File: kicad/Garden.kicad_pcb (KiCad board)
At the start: 2 copper layers, 24 parts, among them J1 EC, J10 FAN_PWM, J11 SPI, J2 TEMP, J3 DHT, J4 PH, J5 Serial, J6 Power, J7 RELAIS, J8 RC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

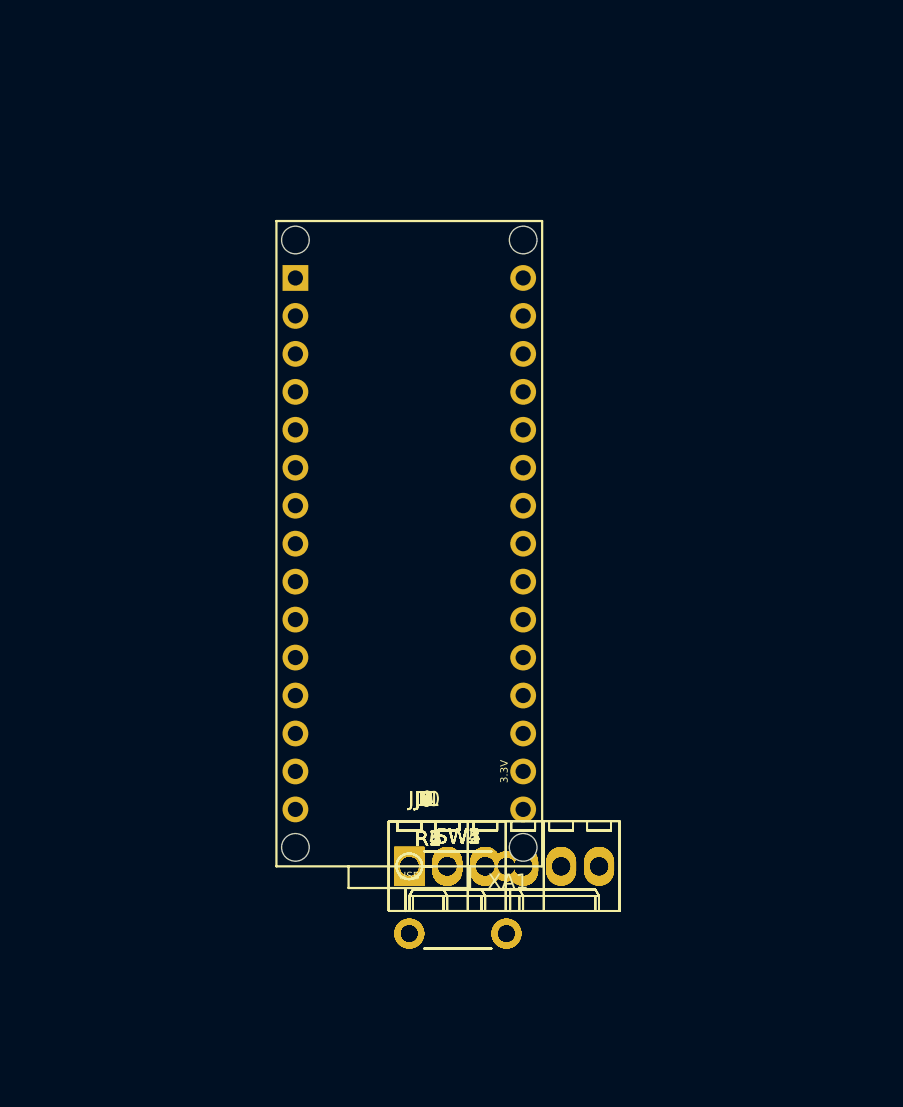
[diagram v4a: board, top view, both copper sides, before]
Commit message: Redesign board layout WIP
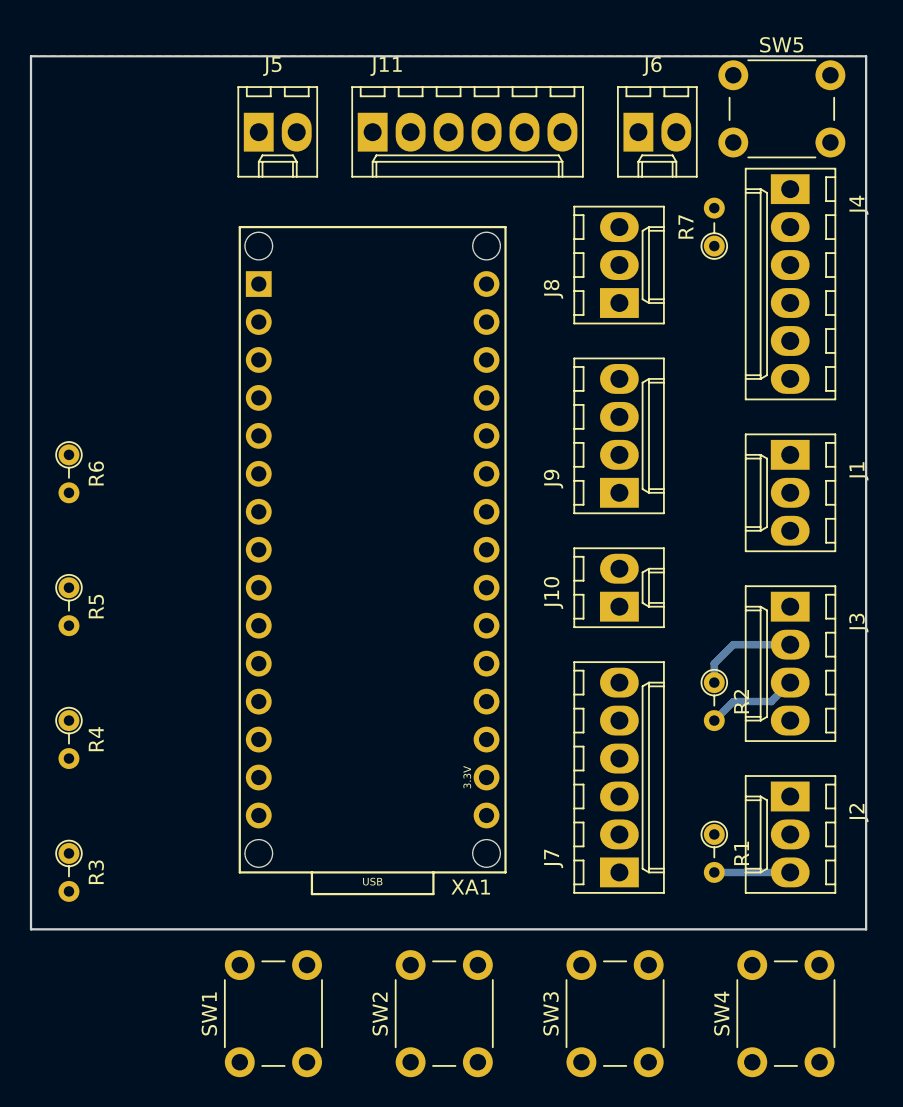
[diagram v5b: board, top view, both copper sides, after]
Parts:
- moved SW5 57.2 mm to (170.2, 52.1)
- moved J4 52.0 mm to (174.0, 59.7), turned to 270 degrees
- moved J6 51.5 mm to (163.8, 55.9)
- moved J5 50.1 mm to (138.4, 55.9)
- moved J11 49.2 mm to (146.1, 55.9)
- moved R7 46.3 mm to (168.9, 63.5), turned to 90 degrees
- moved J8 40.2 mm to (162.6, 67.3), turned to 90 degrees
- moved J1 37.5 mm to (174.0, 77.5), turned to 270 degrees
- moved R6 35.7 mm to (125.7, 77.5), turned to 270 degrees
- moved J3 30.8 mm to (174.0, 87.6), turned to 270 degrees
- moved R5 29.4 mm to (125.7, 86.4), turned to 270 degrees
- moved J9 28.7 mm to (162.6, 80.0), turned to 90 degrees
- moved SW4 26.4 mm to (171.4, 118.1), turned to 90 degrees
- moved J2 25.9 mm to (174.0, 100.3), turned to 270 degrees
- moved R4 24.8 mm to (125.7, 95.2), turned to 270 degrees
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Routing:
- net A0: track 0.00 -> 6.88 mm
- net Net-(J3-Pad3): track 0.00 -> 6.13 mm
- net D3: track 0.00 -> 5.08 mm
- added copper zone on F.Cu, net +5V
- added copper zone on B.Cu, net GND
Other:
- board outline added: 55.9 x 58.4 mm
- net class Default: trace_width 0.25 -> 0.5

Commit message: New pcb design with butons, wip
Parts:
- moved SW4 108.1 mm to (88.9, 48.3)
- moved SW3 91.9 mm to (100.3, 48.3)
- moved R2 86.8 mm to (86.4, 66.0)
- moved SW2 79.0 mm to (111.8, 48.3)
- moved J3 77.6 mm to (96.5, 83.8), turned to 180 degrees
- moved XA1 71.4 mm to (90.2, 61.0), turned to 270 degrees
- moved SW1 71.2 mm to (123.2, 48.3)
- moved J7 68.2 mm to (101.6, 74.9), turned to 180 degrees
- moved J1 67.6 mm to (106.7, 83.8), turned to 180 degrees
- moved R3 59.9 mm to (130.8, 44.5), turned to 90 degrees
- moved J4 55.1 mm to (124.5, 83.8), turned to 180 degrees
- moved J10 54.8 mm to (109.2, 74.9), turned to 180 degrees
- moved R4 51.2 mm to (119.4, 44.5), turned to 90 degrees
- moved R5 45.5 mm to (108.0, 44.5), turned to 90 degrees
- moved R6 44.1 mm to (96.5, 44.5), turned to 90 degrees
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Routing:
- net D13_SCK: track 0.00 -> 59.5 mm
- net D12_MISO: track 0.00 -> 58.7 mm
- net D11_MOSI: track 0.00 -> 55.1 mm
- net D10_CS: track 0.00 -> 52.8 mm
- net RX: track 0.00 -> 17.6 mm
- net TX: track 0.00 -> 14.3 mm
- net Net-(J3-Pad3): track 6.13 -> 17.6 mm
- net A0: track 6.88 -> 0.00 mm
- net D3: track 5.08 -> 11.4 mm
- net D2: track 0.00 -> 3.18 mm
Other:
- board size 55.9 x 58.4 mm -> 61 x 49.5 mm

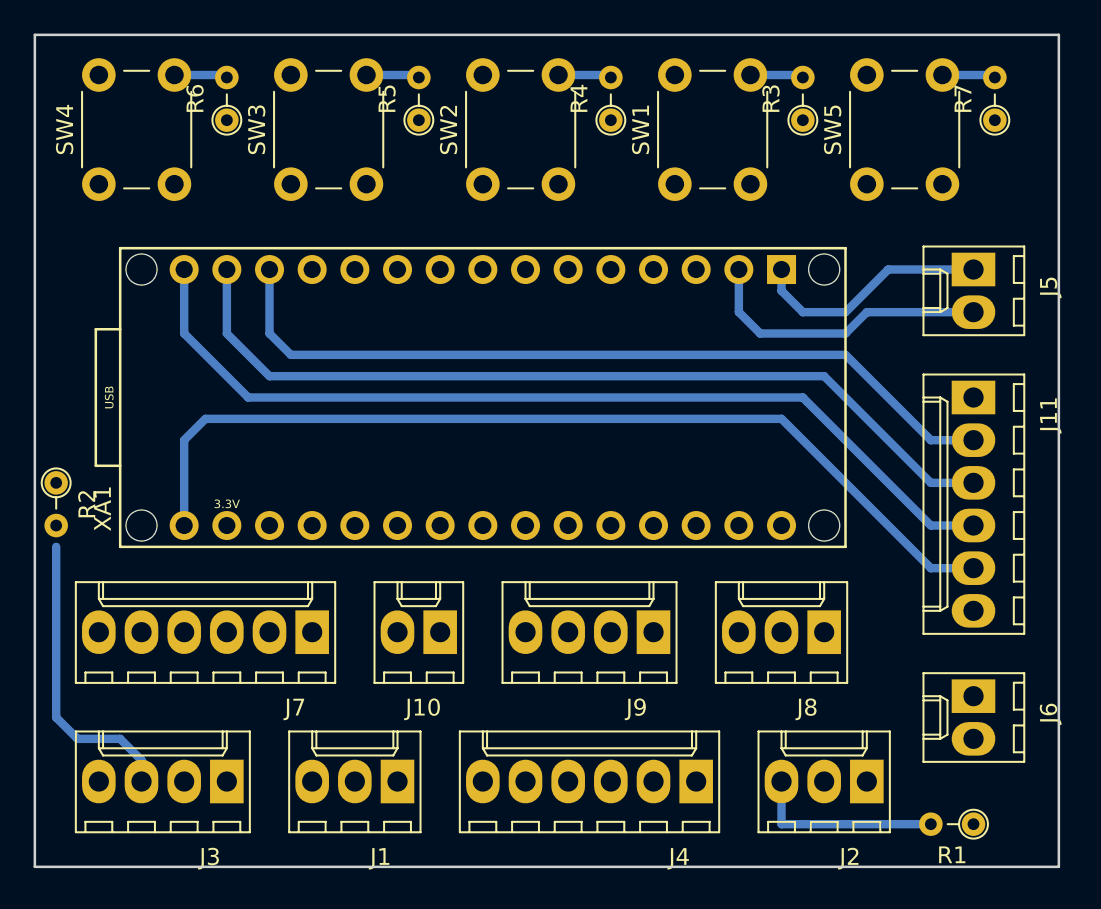
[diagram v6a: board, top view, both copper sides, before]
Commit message: Add missing tracks
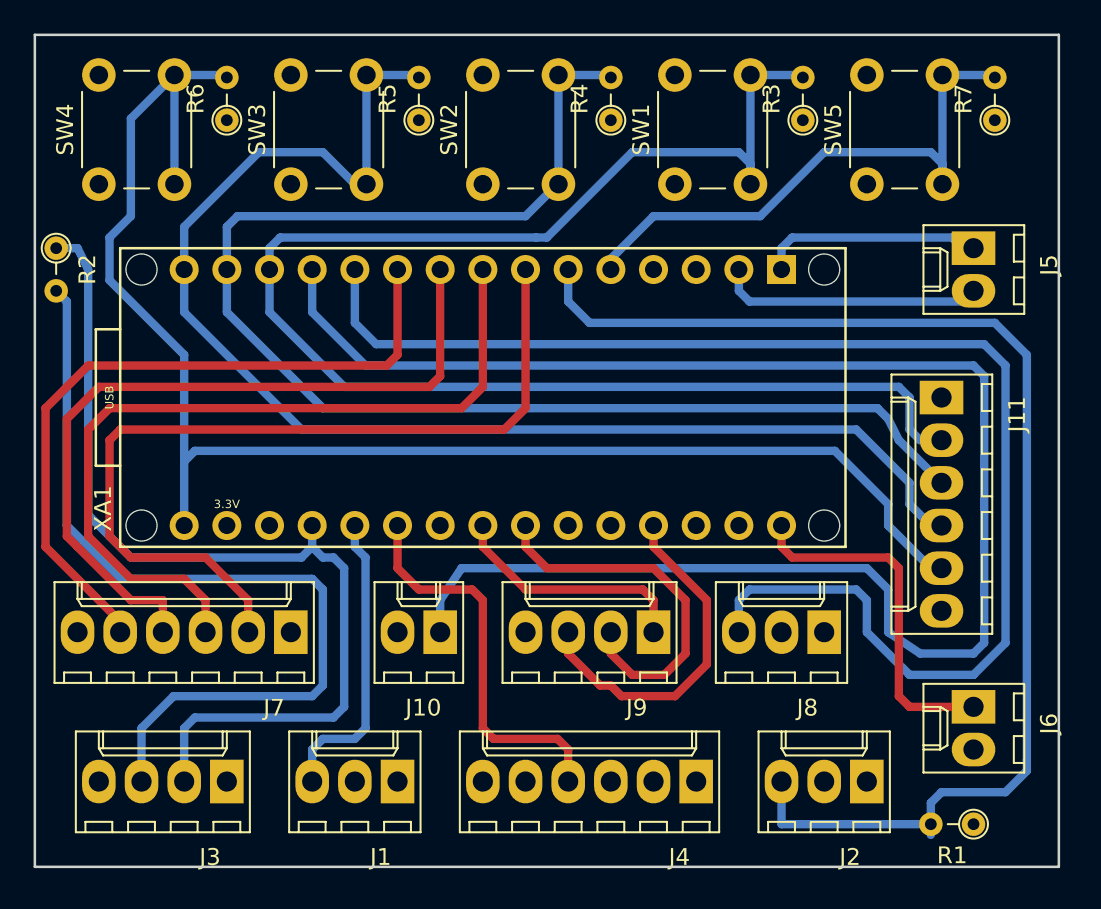
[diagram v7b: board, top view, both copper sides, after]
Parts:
- moved R2 14.0 mm to (86.4, 52.1)
- moved J11 1.91 mm to (139.1, 61.0)
- moved J5 1.27 mm to (141.0, 52.1)
- moved J7 1.27 mm to (100.3, 74.9)
- moved J6 0.64 mm to (141.0, 79.4)
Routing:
- net D9: track 0.00 -> 99.0 mm
- net D8: track 0.00 -> 81.5 mm
- net D3: track 11.4 -> 75.1 mm
- net A0: track 0.00 -> 57.1 mm
- net D4: track 0.00 -> 51.3 mm
- net D5: track 0.00 -> 48.4 mm
- net D6: track 0.00 -> 45.8 mm
- net D7: track 0.00 -> 42.5 mm
- net D10_CS: track 52.8 -> 91.5 mm
- net Net-(J3-Pad3): track 17.6 -> 51.8 mm
- net D2: track 3.18 -> 34.2 mm
- net D13_SCK: track 59.5 -> 88.9 mm
- net D11_MOSI: track 55.1 -> 83.5 mm
- net A2: track 0.00 -> 23.5 mm
- net A5: track 0.00 -> 22.1 mm
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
